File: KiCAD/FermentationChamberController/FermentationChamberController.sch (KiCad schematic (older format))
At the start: 7 parts, among them P1 Digital, P2 Analog

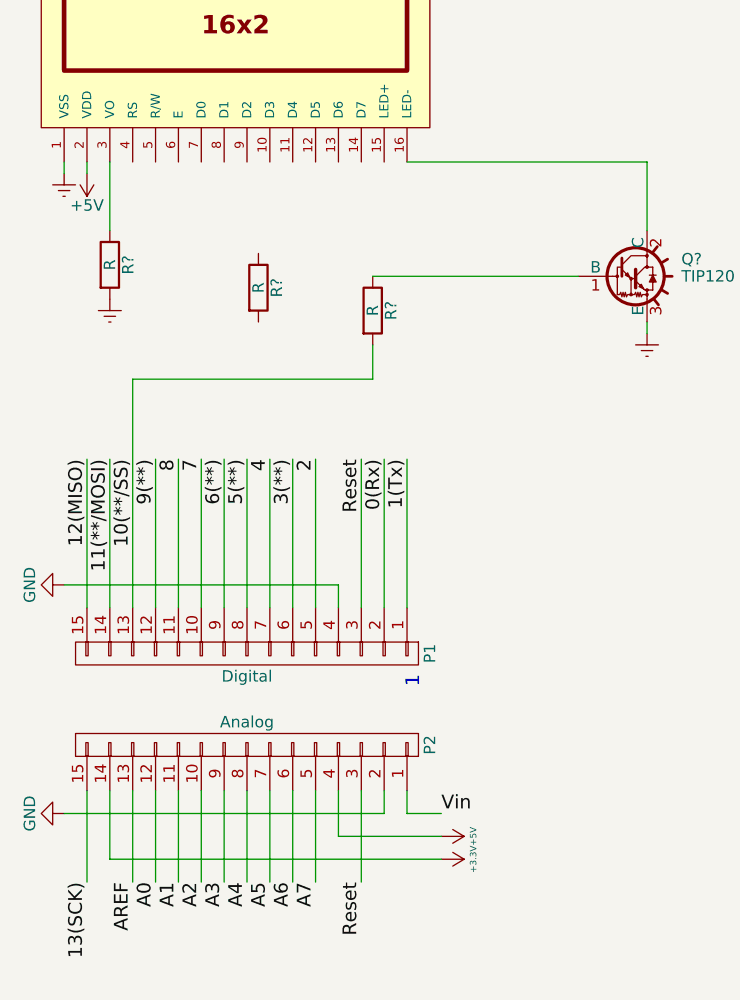
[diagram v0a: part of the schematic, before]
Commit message: Minor updates to lcd schematic
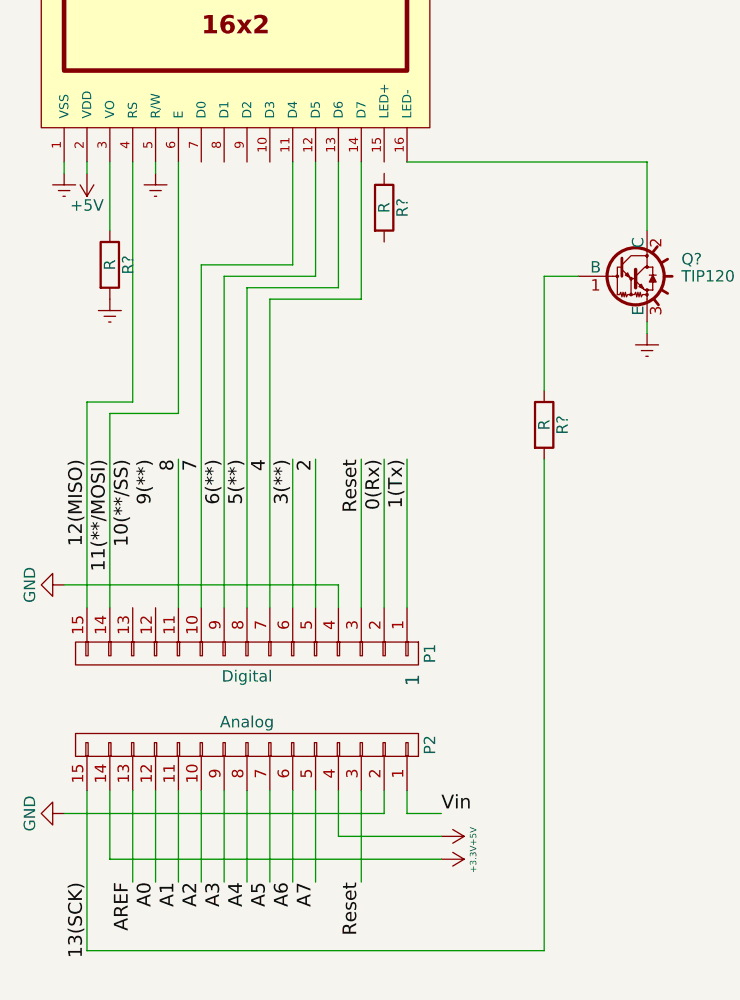
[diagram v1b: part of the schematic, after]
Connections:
- net 10(**/SS): no longer P1.13 (P13), R?.2
- net 11(**/MOSI): now also DS?.6 (E)
- net 12(MISO): now also DS?.4 (RS)
- net 13(SCK): now also R?.2
- net 4: now also DS?.14 (D7)
- net 5(**): now also DS?.13 (D6)
- net 6(**): now also DS?.12 (D5)
- net 7: now also DS?.11 (D4)
- net 9(**): no longer P1.12 (P12)
- net Earth: now also DS?.5 (R/W)
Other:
- moved on the sheet: R?
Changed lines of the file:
@@
 L R R?
 U 1 1 591B3EE1
-P 3600 2200
-F 0 "R?" V 3680 2200 50  0000 C CNN
-F 1 "R" V 3600 2200 50  0000 C CNN
-F 2 "" V 3530 2200 50  0001 C CNN
-F 3 "" H 3600 2200 50  0001 C CNN
-	1    3600 2200
+P 4150 1850
+F 0 "R?" V 4230 1850 50  0000 C CNN
+F 1 "R" V 4150 1850 50  0000 C CNN
+F 2 "" V 4080 1850 50  0001 C CNN
+F 3 "" H 4150 1850 50  0001 C CNN
+	1    4150 1850
 	1    0    0    -1
 $EndComp
@@
 L R R?
 U 1 1 591B3F3C
-P 4100 2300
-F 0 "R?" V 4180 2300 50  0000 C CNN
-F 1 "R" V 4100 2300 50  0000 C CNN
-F 2 "" V 4030 2300 50  0001 C CNN
-F 3 "" H 4100 2300 50  0001 C CNN
-	1    4100 2300
+P 4850 2800
+F 0 "R?" V 4930 2800 50  0000 C CNN
+F 1 "R" V 4850 2800 50  0000 C CNN
+F 2 "" V 4780 2800 50  0001 C CNN
+F 3 "" H 4850 2800 50  0001 C CNN
+	1    4850 2800
 	1    0    0    -1
 $EndComp
@@
 	3750 3600 3750 2950
 Wire Wire Line
-	3650 2950 3650 3600
+	3650 2250 3650 3600
 Wire Wire Line
-	3550 3600 3550 2950
+	3550 2200 3550 3600
 Wire Wire Line
-	3450 2950 3450 3600
+	3450 2150 3450 3600
 Wire Wire Line
-	3350 3600 3350 2950
+	3350 2100 3350 3600
 Wire Wire Line
 	3250 2950 3250 3600
 Wire Wire Line
-	3150 3600 3150 2950
+	2950 2750 2950 3600
 Wire Wire Line
-	3050 2600 3050 3600
-Wire Wire Line
-	2950 3600 2950 2950
-Wire Wire Line
-	2850 2950 2850 3600
+	2850 2700 2850 3600
 Wire Wire Line
 	2750 4500 4150 4500
@@
 	3050 4800 3050 4400
 Wire Wire Line
-	2850 4400 2850 4800
+	2850 4400 2850 5100
 Wire Wire Line
 	4250 1650 5300 1650
 Wire Wire Line
 	5300 1650 5300 1950
-Wire Wire Line
-	5000 2150 4100 2150
-Wire Wire Line
-	4100 2450 4100 2600
-Wire Wire Line
-	4100 2600 3050 2600
 $Comp
 L Earth #PWR?
@@
 	1    0    0    -1
 $EndComp
+Wire Wire Line
+	3050 1650 3050 2700
+Wire Wire Line
+	3050 2700 2850 2700
+Wire Wire Line
+	5000 2150 4850 2150
+Wire Wire Line
+	4850 2150 4850 2650
+Wire Wire Line
+	4850 2950 4850 5100
+Wire Wire Line
+	4850 5100 2850 5100
+$Comp
+L Earth #PWR?
+U 1 1 591B5084
+P 3150 1700
+F 0 "#PWR?" H 3150 1450 50  0001 C CNN
+F 1 "Earth" H 3150 1550 50  0001 C CNN
+F 2 "" H 3150 1700 50  0001 C CNN
+F 3 "" H 3150 1700 50  0001 C CNN
+	1    3150 1700
+	1    0    0    -1
+$EndComp
+Wire Wire Line
+	3150 1650 3150 1700
+Wire Wire Line
+	3250 1650 3250 2750
+Wire Wire Line
+	3250 2750 2950 2750
+Wire Wire Line
+	3750 1650 3750 2100
+Wire Wire Line
+	3750 2100 3350 2100
+Wire Wire Line
+	3850 1650 3850 2150
+Wire Wire Line
+	3850 2150 3450 2150
+Wire Wire Line
+	3950 1650 3950 2200
+Wire Wire Line
+	3950 2200 3550 2200
+Wire Wire Line
+	4050 1650 4050 2250
+Wire Wire Line
+	4050 2250 3650 2250
 $EndSCHEMATC

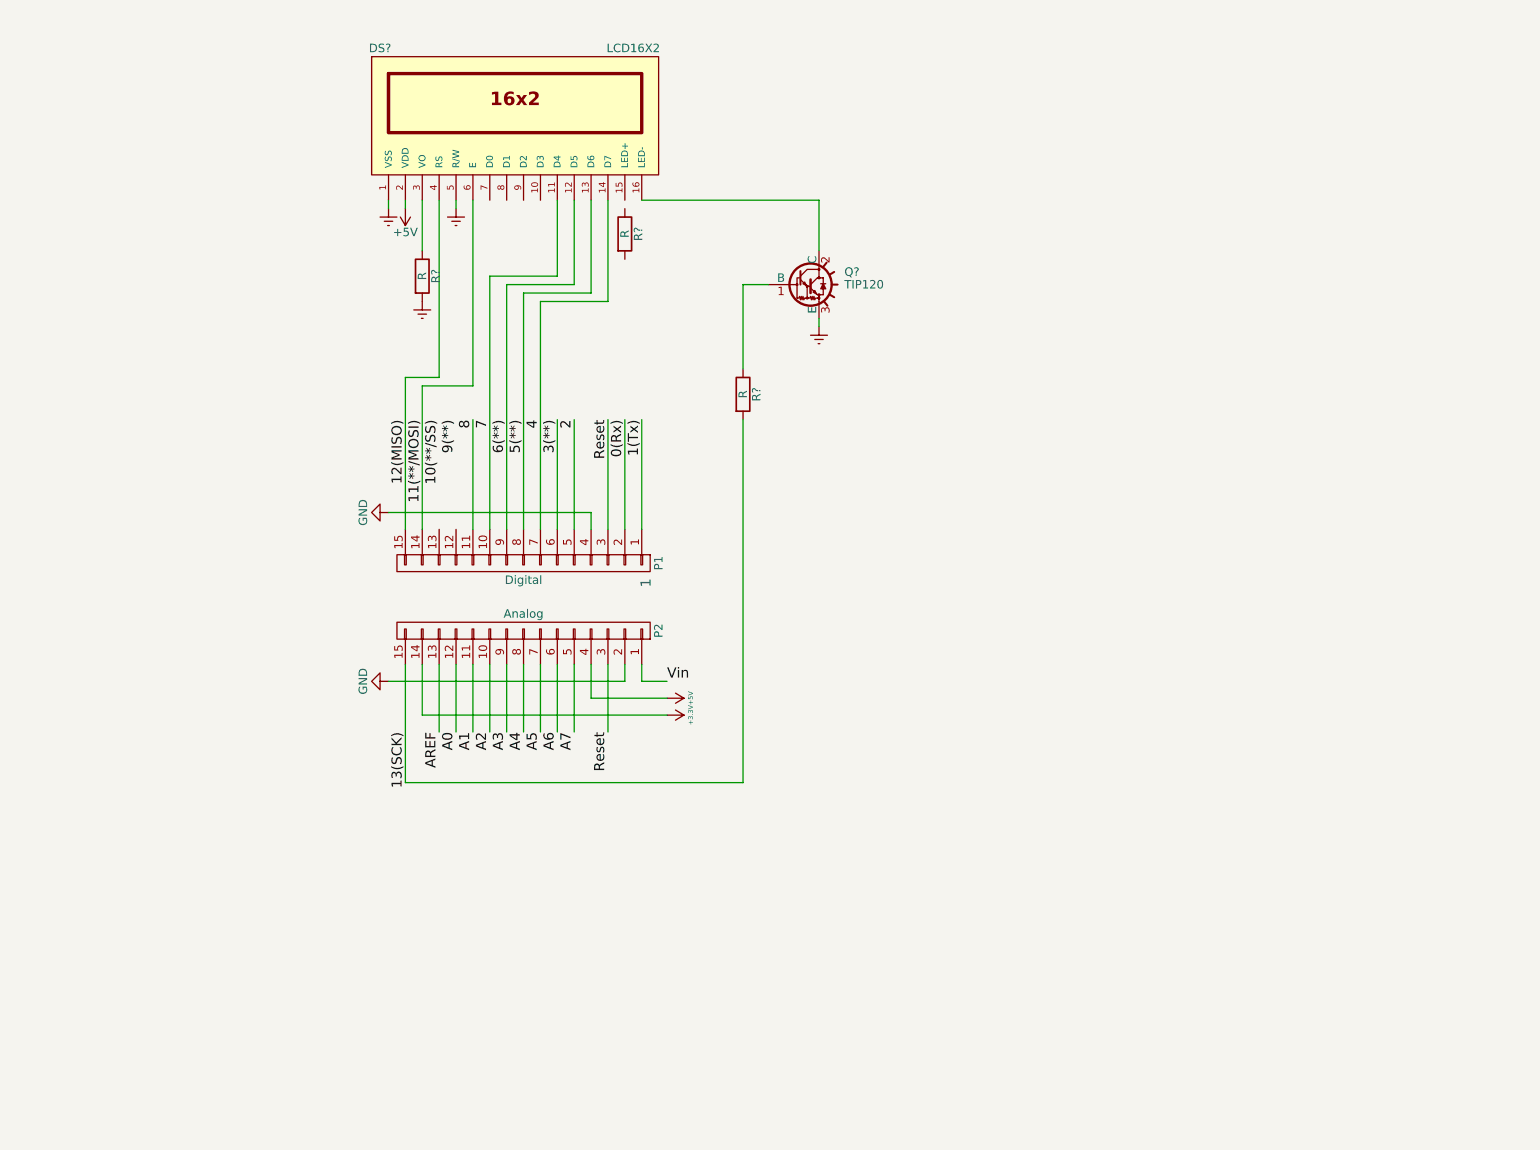
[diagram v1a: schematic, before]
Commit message: Basic schematic complete per Fritzing file
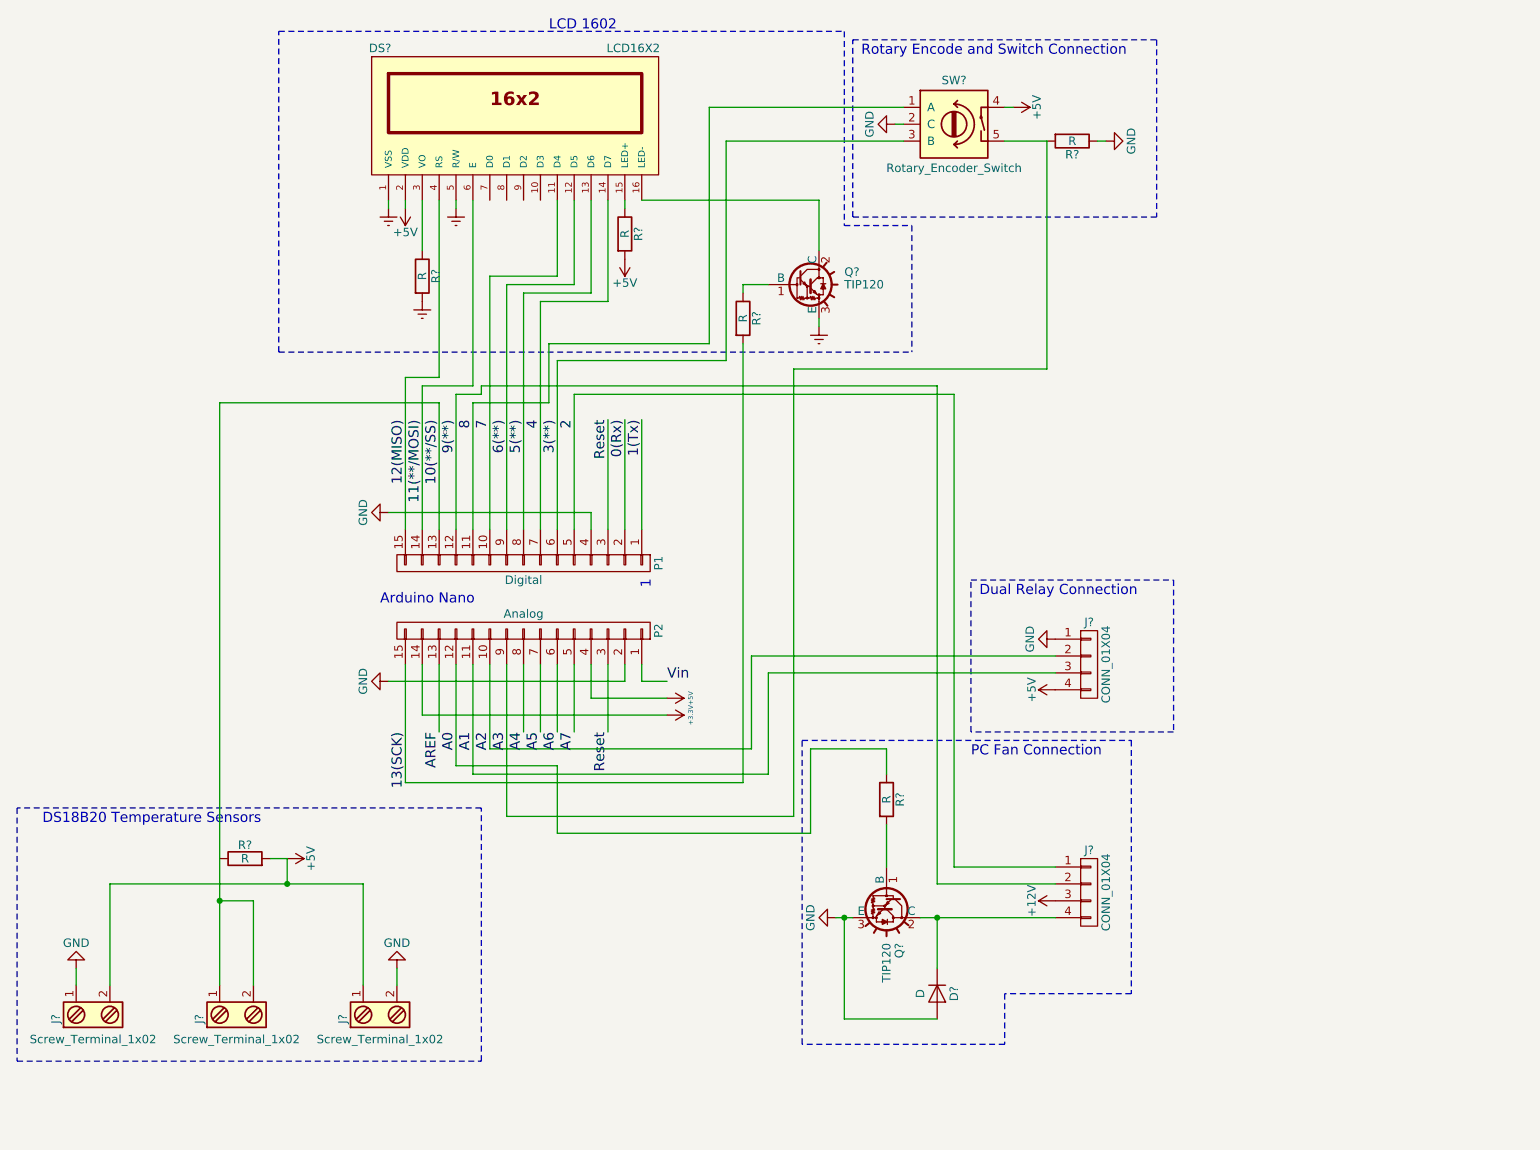
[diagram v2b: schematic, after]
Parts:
- added D?: D, symbol D
- added J? (x3): Screw_Terminal_1x02, symbol Screw_Terminal_1x02
- added J? (x2): CONN_01X04, symbol CONN_01X04
- added Q?: TIP120, TO_SOT_Packages_THT:TO-220_Vertical, symbol TIP120
- added R? (x3): R, symbol R
- added SW?: Rotary_Encoder_Switch, symbol Rotary_Encoder_Switch
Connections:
- net +5V: now also R?.2, J?.1, J?.2, J?.4 (P4), R?.2, SW?.4
- net 10(**/SS): now also P1.13 (P13), J?.1, J?.2
- net 2: now also J?.1 (P1)
- net 3(**): now also SW?.3 (B)
- net 8: now also SW?.1 (A)
- net 9(**): now also P1.12 (P12), J?.2 (P2)
- net A0: now also R?.1
- net A1: now also J?.3 (P3)
- net A2: now also J?.2 (P2)
- net A3: now also R?.2, SW?.5
- net GND: now also D?.2 (A), J?.1, J?.1 (P1), J?.2, Q?.3 (E), R?.1, SW?.2 (C)
- net at DS?.15 (LED+): now also R?.1
- new net: D?.1 (K), J?.4 (P4), Q?.2 (C)
- new net: Q?.1 (B), R?.2
- new net +12V: J?.3 (P3)
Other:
- note added: "Arduino Nano"
- note added: "DS18B20 Temperature Sensors"
- note added: "Dual Relay Connection"
- note added: "LCD 1602"
- note added: "PC Fan Connection"
- note added: "Rotary Encode and Switch Connection"
- moved on the sheet: R?

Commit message: Minor schematic fixes (fan diode)
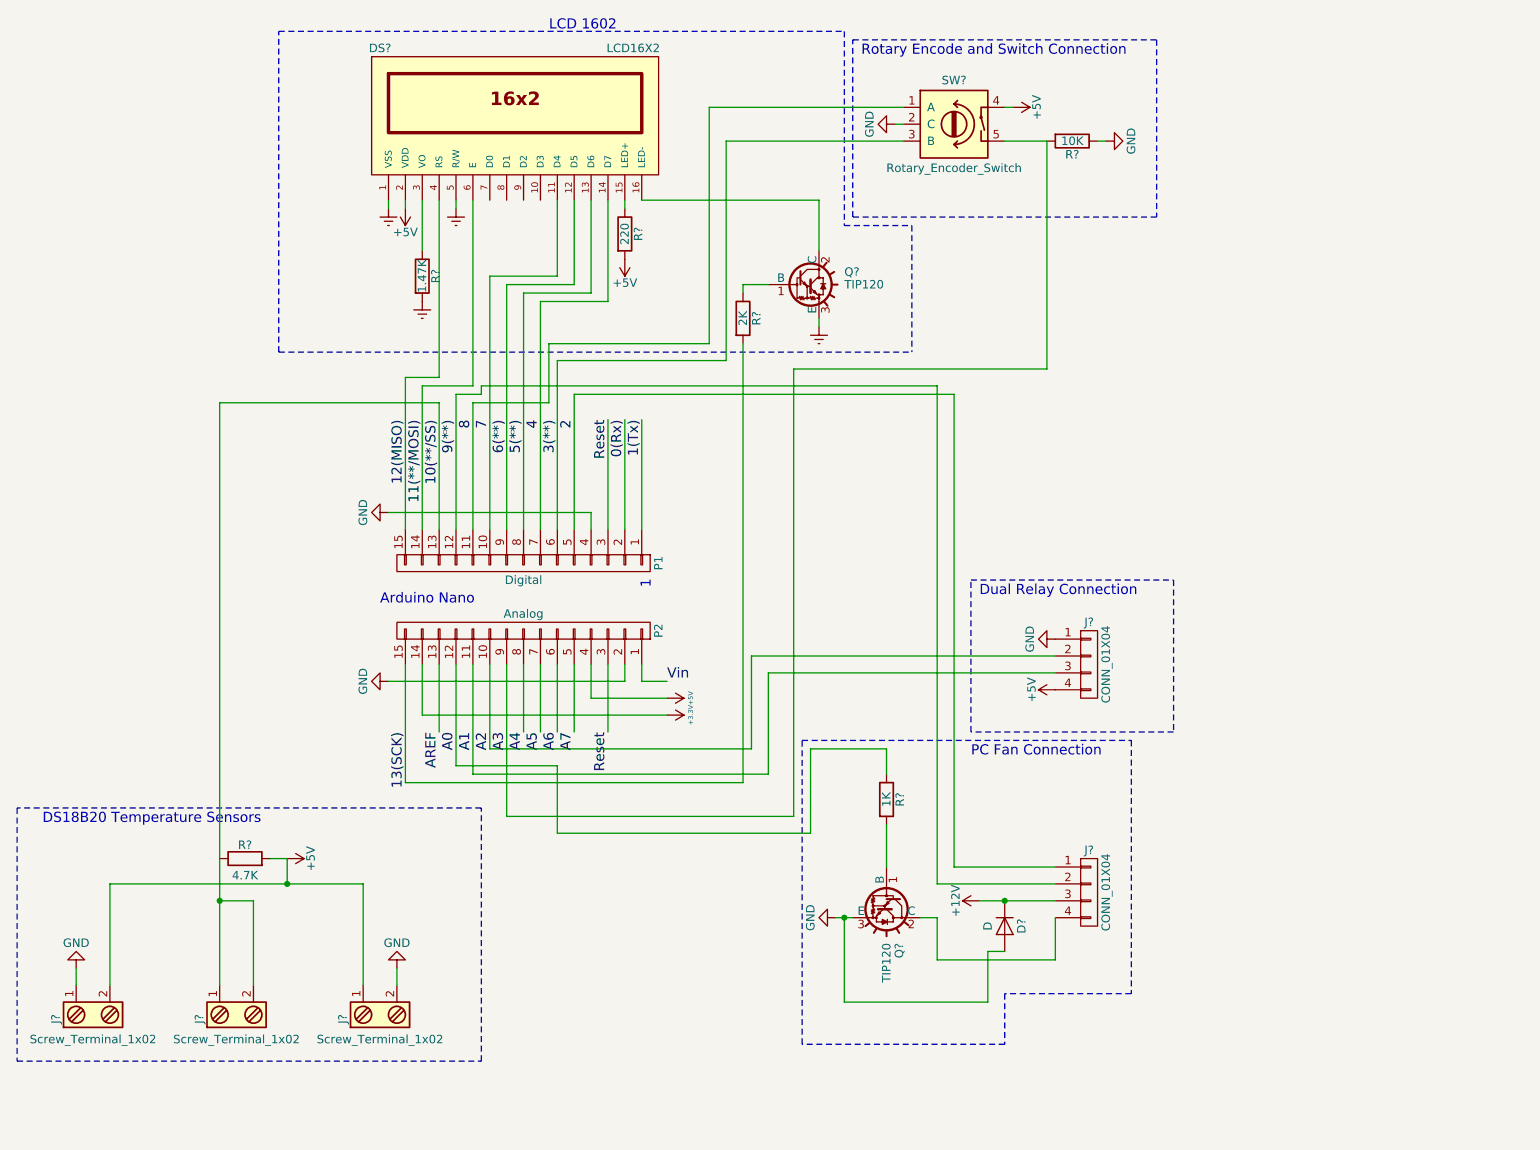
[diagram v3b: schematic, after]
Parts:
- R?: value R -> 1.47K
- R?: value R -> 220
- R?: value R -> 2K
- R?: value R -> 10K
- R?: value R -> 4.7K
- R?: value R -> 1K
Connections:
- net +12V: now also D?.1 (K)
- net at J?.4 (P4), Q?.2 (C): no longer D?.1 (K)
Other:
- moved on the sheet: D?
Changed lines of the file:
@@
 P 2950 2100
 F 0 "R?" V 3030 2100 50  0000 C CNN
-F 1 "R" V 2950 2100 50  0000 C CNN
+F 1 "1.47K" V 2950 2100 50  0000 C CNN
 F 2 "" V 2880 2100 50  0001 C CNN
 F 3 "" H 2950 2100 50  0001 C CNN
@@
 P 4150 1850
 F 0 "R?" V 4230 1850 50  0000 C CNN
-F 1 "R" V 4150 1850 50  0000 C CNN
+F 1 "220" V 4150 1850 50  0000 C CNN
 F 2 "" V 4080 1850 50  0001 C CNN
 F 3 "" H 4150 1850 50  0001 C CNN
@@
 P 4850 2350
 F 0 "R?" V 4930 2350 50  0000 C CNN
-F 1 "R" V 4850 2350 50  0000 C CNN
+F 1 "2K" V 4850 2350 50  0000 C CNN
 F 2 "" V 4780 2350 50  0001 C CNN
 F 3 "" H 4850 2350 50  0001 C CNN
@@
 P 6800 1300
 F 0 "R?" V 6880 1300 50  0000 C CNN
-F 1 "R" V 6800 1300 50  0000 C CNN
+F 1 "10K" V 6800 1300 50  0000 C CNN
 F 2 "" V 6730 1300 50  0001 C CNN
 F 3 "" H 6800 1300 50  0001 C CNN
@@
 P 1900 5550
 F 0 "R?" V 1980 5550 50  0000 C CNN
-F 1 "R" V 1900 5550 50  0000 C CNN
+F 1 "4.7K" V 1800 5550 50  0000 C CNN
 F 2 "" V 1830 5550 50  0001 C CNN
 F 3 "" H 1900 5550 50  0001 C CNN
@@
 L D D?
 U 1 1 591BC636
-P 6000 6350
-F 0 "D?" H 6000 6450 50  0000 C CNN
-F 1 "D" H 6000 6250 50  0000 C CNN
-F 2 "" H 6000 6350 50  0001 C CNN
-F 3 "" H 6000 6350 50  0001 C CNN
-	1    6000 6350
+P 6400 5950
+F 0 "D?" H 6400 6050 50  0000 C CNN
+F 1 "D" H 6400 5850 50  0000 C CNN
+F 2 "" H 6400 5950 50  0001 C CNN
+F 3 "" H 6400 5950 50  0001 C CNN
+	1    6400 5950
 	0    1    1    0
 $EndComp
@@
 P 5700 5200
 F 0 "R?" V 5780 5200 50  0000 C CNN
-F 1 "R" V 5700 5200 50  0000 C CNN
+F 1 "1K" V 5700 5200 50  0000 C CNN
 F 2 "" V 5630 5200 50  0001 C CNN
 F 3 "" H 5700 5200 50  0001 C CNN
@@
 	5400 5900 5500 5900
 Wire Wire Line
-	5900 5900 6700 5900
+	5900 5900 6000 5900
 Wire Wire Line
 	5700 5350 5700 5600
 Wire Wire Line
 	5700 4900 5700 5050
-Wire Wire Line
-	6000 6500 5450 6500
-Wire Wire Line
-	5450 6500 5450 5900
 Connection ~ 5450 5900
 Wire Wire Line
-	6000 6200 6000 5900
-Wire Wire Line
 	5700 4900 5250 4900
 Wire Wire Line
@@
 Wire Wire Line
 	3750 5000 3150 5000
-Connection ~ 6000 5900
-$Comp
-L +12V #PWR?
-U 1 1 591BD56B
-P 6700 5800
-F 0 "#PWR?" H 6700 5650 50  0001 C CNN
-F 1 "+12V" H 6700 5940 50  0000 C CNN
-F 2 "" H 6700 5800 50  0001 C CNN
-F 3 "" H 6700 5800 50  0001 C CNN
-	1    6700 5800
-	0    -1   -1   0
-$EndComp
 Wire Wire Line
 	6700 5700 6000 5700
@@
 Text Notes 2700 4050 0    60   ~ 0
 Arduino Nano
+$Comp
+L +12V #PWR?
+U 1 1 591BFE81
+P 6250 5800
+F 0 "#PWR?" H 6250 5650 50  0001 C CNN
+F 1 "+12V" H 6250 5940 50  0000 C CNN
+F 2 "" H 6250 5800 50  0001 C CNN
+F 3 "" H 6250 5800 50  0001 C CNN
+	1    6250 5800
+	0    -1   -1   0
+$EndComp
+Wire Wire Line
+	6250 5800 6700 5800
+Connection ~ 6400 5800
+Wire Wire Line
+	5450 5900 5450 6400
+Wire Wire Line
+	5450 6400 6300 6400
+Wire Wire Line
+	6300 6400 6300 6100
+Wire Wire Line
+	6300 6100 6400 6100
+Wire Wire Line
+	6700 5900 6700 6150
+Wire Wire Line
+	6700 6150 6000 6150
+Wire Wire Line
+	6000 6150 6000 5900
 $EndSCHEMATC
